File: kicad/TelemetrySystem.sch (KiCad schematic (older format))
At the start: 5 parts

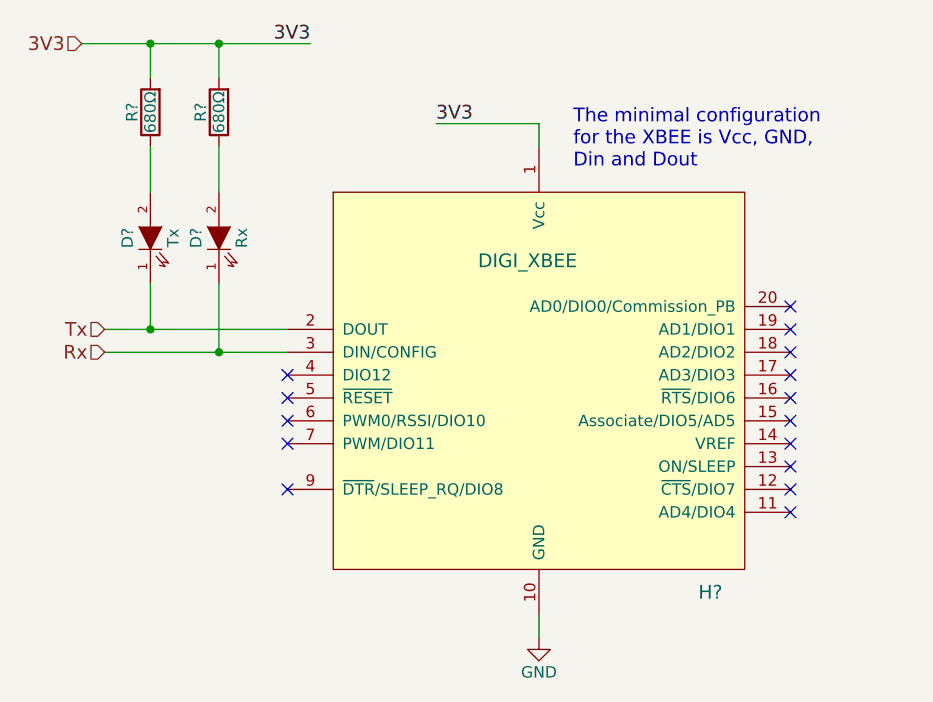
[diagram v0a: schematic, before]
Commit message: Completed the new schematic (draft) and started the layout to verify the design
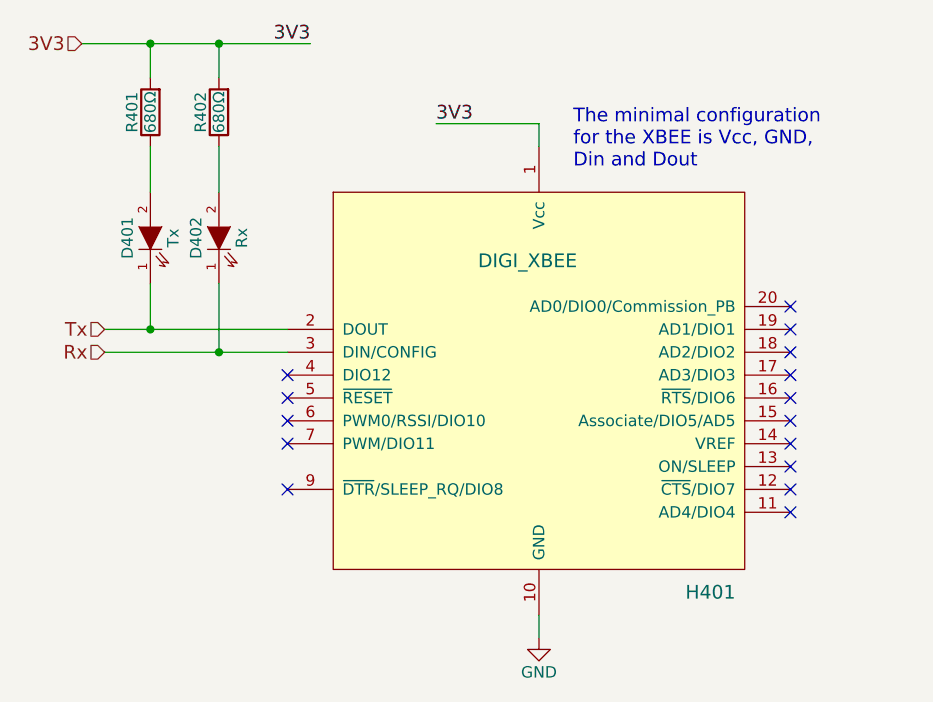
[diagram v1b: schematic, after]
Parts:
- gave numbers to parts that had none: 5
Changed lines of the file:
@@
 $Descr A4 11693 8268
 encoding utf-8
-Sheet 5 6
+Sheet 4 5
 Title ""
 Date ""
@@
 $EndDescr
 $Comp
-L DIGI_XBEE H?
+L DIGI_XBEE H401
 U 1 1 5A7121A6
 P 5050 3200
-F 0 "H?" H 5800 2300 60  0000 C CNN
+F 0 "H401" H 5800 2300 60  0000 C CNN
 F 1 "DIGI_XBEE" H 5000 3750 60  0000 C CNN
 F 2 "FieldDevice_Footprints:XBEE_S2C" H 4400 3000 60  0001 C CNN
@@
 $EndComp
 $Comp
-L GND #PWR?
+L GND #PWR09
 U 1 1 5A7121AD
 P 5050 4300
-F 0 "#PWR?" H 5050 4050 50  0001 C CNN
+F 0 "#PWR09" H 5050 4050 50  0001 C CNN
 F 1 "GND" H 5050 4150 50  0000 C CNN
 F 2 "" H 5050 4300 50  0000 C CNN
@@
 NoConn ~ 3950 3250
 $Comp
-L LED-RESCUE-FieldDevice D?
+L LED-RESCUE-FieldDevice D401
 U 1 1 5A7121C4
 P 3350 2550
-F 0 "D?" H 3350 2650 50  0000 C CNN
+F 0 "D401" H 3350 2650 50  0000 C CNN
 F 1 "Tx" H 3350 2450 50  0000 C CNN
 F 2 "Diodes_SMD:D_0805" H 3350 2550 60  0001 C CNN
@@
 $EndComp
 $Comp
-L LED-RESCUE-FieldDevice D?
+L LED-RESCUE-FieldDevice D402
 U 1 1 5A7121CB
 P 3650 2550
-F 0 "D?" H 3650 2650 50  0000 C CNN
+F 0 "D402" H 3650 2650 50  0000 C CNN
 F 1 "Rx" H 3650 2450 50  0000 C CNN
 F 2 "Diodes_SMD:D_0805" H 3650 2550 60  0001 C CNN
@@
 $EndComp
 $Comp
-L R R?
+L R R401
 U 1 1 5A7121D2
 P 3350 2000
-F 0 "R?" V 3430 2000 50  0000 C CNN
+F 0 "R401" V 3430 2000 50  0000 C CNN
 F 1 "680Ω" V 3350 2000 50  0000 C CNN
 F 2 "Resistors_SMD:R_0805_HandSoldering" V 3280 2000 50  0001 C CNN
@@
 $EndComp
 $Comp
-L R R?
+L R R402
 U 1 1 5A7121D9
 P 3650 2000
-F 0 "R?" V 3730 2000 50  0000 C CNN
+F 0 "R402" V 3730 2000 50  0000 C CNN
 F 1 "680Ω" V 3650 2000 50  0000 C CNN
 F 2 "Resistors_SMD:R_0805_HandSoldering" V 3580 2000 50  0001 C CNN

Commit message: More changes to the layout for the Power System integration
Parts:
- R401, R402: footprint Resistors_SMD:R_0805_HandSoldering -> Resistors_SMD:R_0805
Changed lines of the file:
@@
 F 0 "R401" V 3430 2000 50  0000 C CNN
 F 1 "680Ω" V 3350 2000 50  0000 C CNN
-F 2 "Resistors_SMD:R_0805_HandSoldering" V 3280 2000 50  0001 C CNN
+F 2 "Resistors_SMD:R_0805" V 3280 2000 50  0001 C CNN
 F 3 "" H 3350 2000 50  0000 C CNN
 	1    3350 2000
@@
 F 0 "R402" V 3730 2000 50  0000 C CNN
 F 1 "680Ω" V 3650 2000 50  0000 C CNN
-F 2 "Resistors_SMD:R_0805_HandSoldering" V 3580 2000 50  0001 C CNN
+F 2 "Resistors_SMD:R_0805" V 3580 2000 50  0001 C CNN
 F 3 "" H 3650 2000 50  0000 C CNN
 	1    3650 2000
